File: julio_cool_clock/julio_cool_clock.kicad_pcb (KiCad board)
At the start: 2 copper layers, 140 x 90 mm, 40 parts, among them J1 PJ-102AH, J2 Conn_02x03_Odd_Even, SW1 Omron_B3F_SPST, SW2 Omron_B3F_SPST, SW3 Omron_B3F_SPST, SW4 Omron_B3F_SPST, U1 ATmega328-PU, U2 MAX7219, U3 DS1307_DIP-8, Y1 Crystal_16MHz, Y2 Crystal_32768Hz

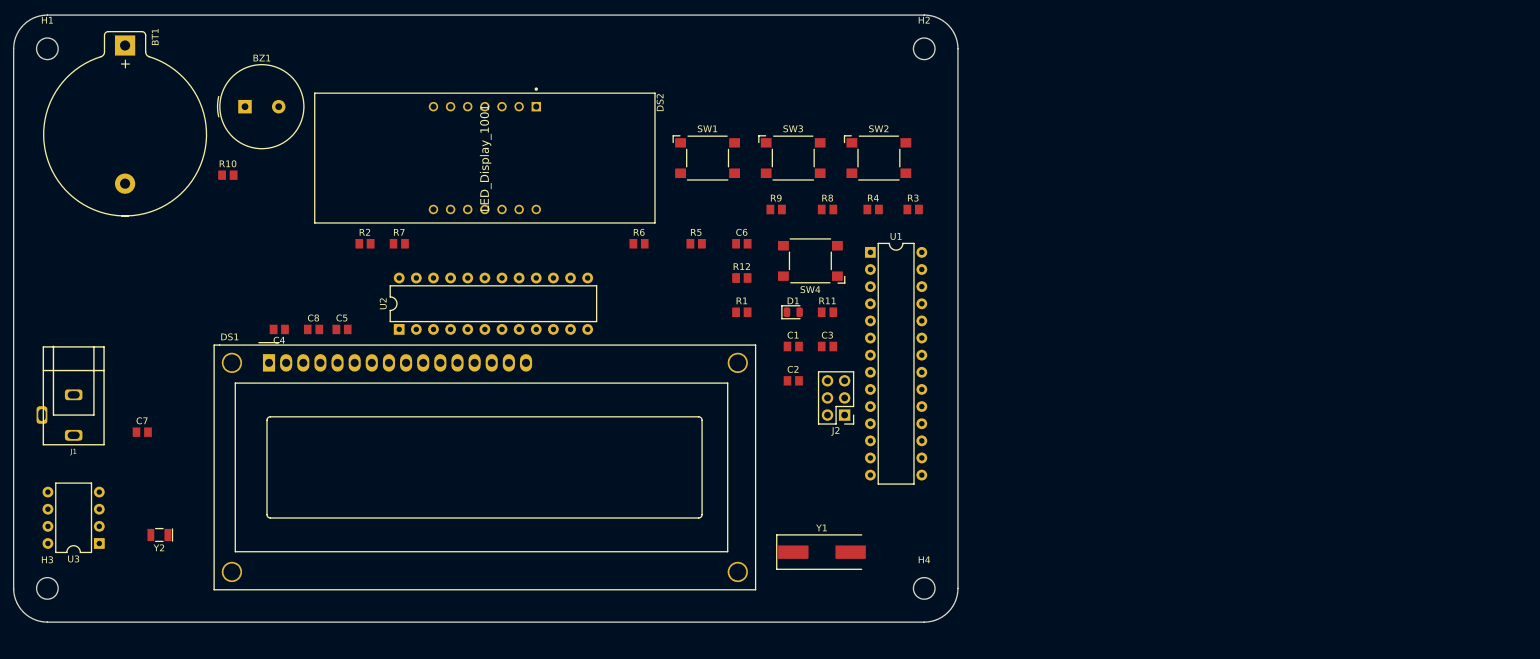
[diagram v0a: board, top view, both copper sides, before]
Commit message: Design Commit 5
Pushed Netlist to PCB and made initial placement of all components, including UI components.
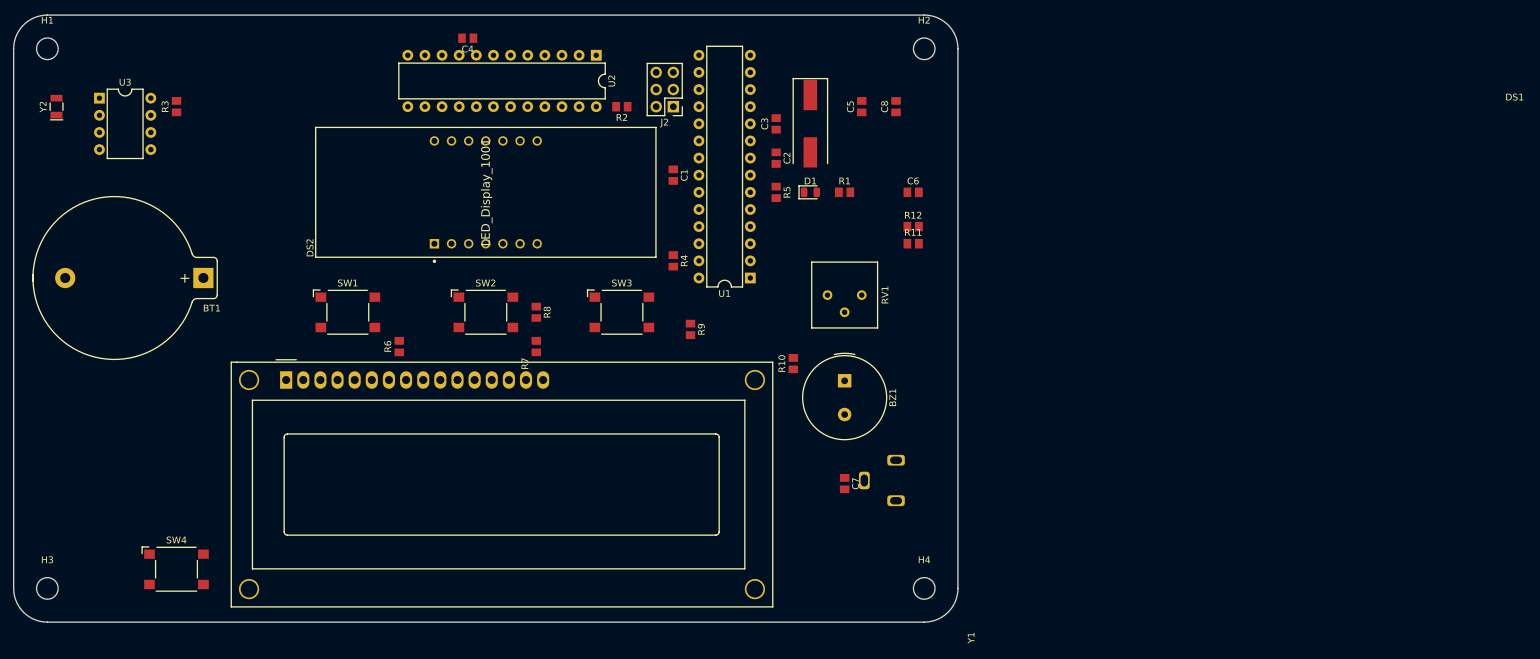
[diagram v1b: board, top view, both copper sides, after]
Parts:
- added RV1: R_POT_10K, footprints:Potentiometer_Bourns_3386P_Vertical, F.Cu at (200.7, 96.5)
- J1: moved to B.Cu
- moved J1 122.3 mm to (210.8, 124.0)
- moved R3 110.3 mm to (104.1, 68.6), turned to 90 degrees
- moved SW4 104.5 mm to (104.1, 137.2), turned to 0 degrees
- moved C7 104.4 mm to (203.2, 124.5), turned to -90 degrees
- moved BZ1 97.7 mm to (203.2, 109.2), turned to -90 degrees
- moved C8 92.5 mm to (210.8, 68.6), turned to 90 degrees
- moved R10 88.4 mm to (195.6, 106.7), turned to 90 degrees
- moved C5 83.8 mm to (205.7, 68.6), turned to 90 degrees
- moved U3 66.0 mm to (92.7, 67.3), turned to 0 degrees
- moved Y2 65.3 mm to (86.4, 68.6), turned to 90 degrees
- moved Y1 63.5 mm to (198.1, 71.1), turned to -90 degrees
- moved SW2 62.6 mm to (150.0, 99.1)
- moved SW1 58.0 mm to (129.5, 99.1)
- moved J2 52.3 mm to (177.8, 68.6)
- moved C4 51.4 mm to (147.3, 58.4)
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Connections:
- net Net-(C6-Pad2) renamed /RTS
- net Net-(J3-Pad4) renamed /SER_TX
- net Net-(J3-Pad5) renamed /SER_RX
- DS1 pad 3: POTENTIOMETER -> Net-(DS1-Pad3)
